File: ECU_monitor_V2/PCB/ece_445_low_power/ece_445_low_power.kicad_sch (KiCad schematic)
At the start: 59 parts, among them J1 Conn_01x02, J2 Conn_01x02, J3 Conn_02x02_Counter_Clockwise, J4 Conn_01x02, J5 LED, J6 ISP, Q1 2N7000, U1 LM393, U2 Si8640BD-B-IS2, U3 ATtiny85-20S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

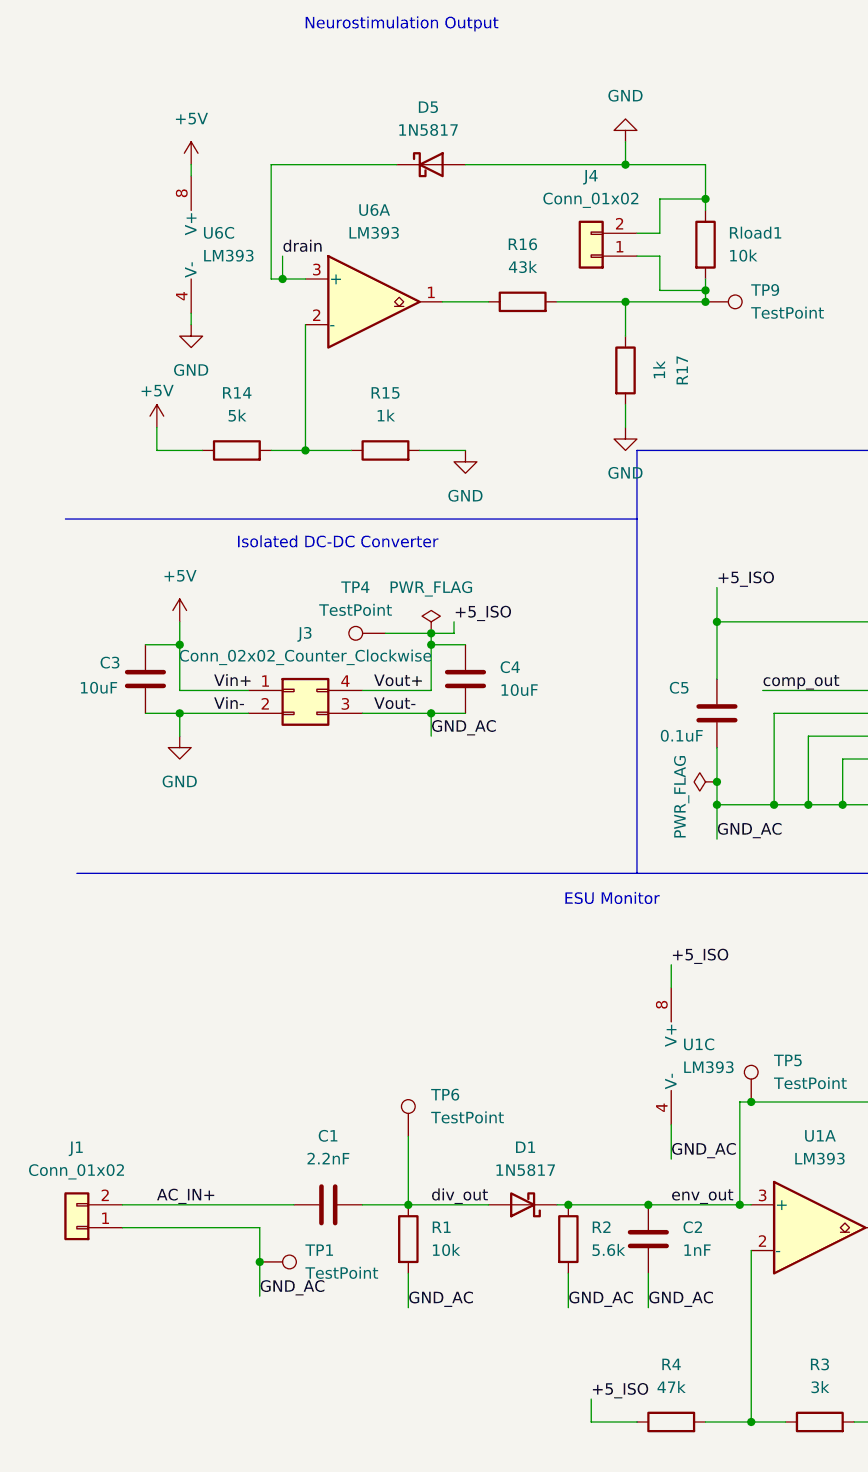
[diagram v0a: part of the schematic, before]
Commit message: Updated Low Power PCB, added missing 1k resistor to +5V in output
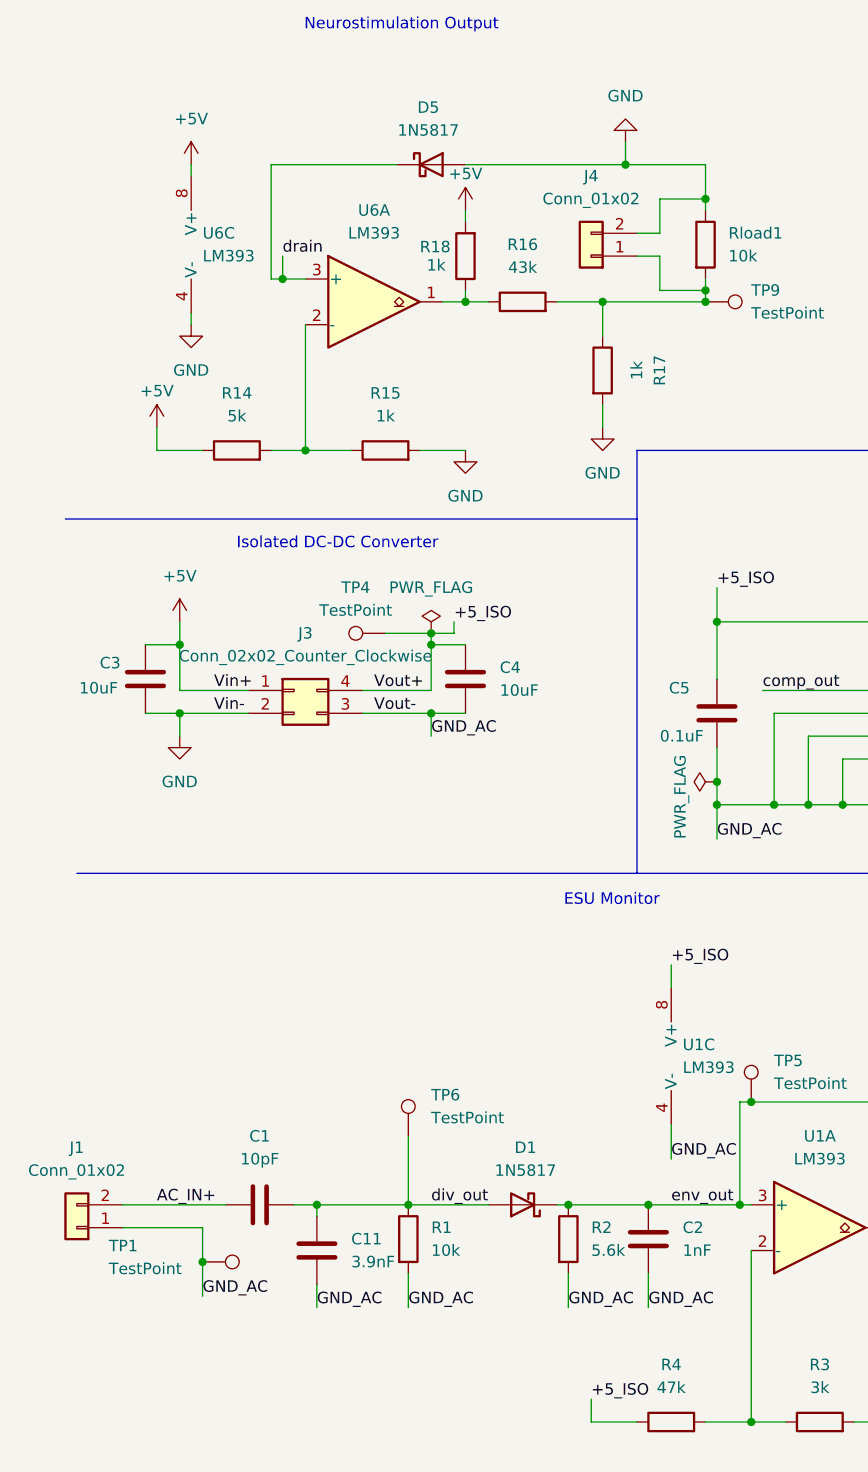
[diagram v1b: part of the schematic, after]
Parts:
- added C11: 3.9nF, Capacitor_THT:C_Disc_D4.7mm_W2.5mm_P5.00mm, symbol Device:C
- added R18: 1k, Resistor_THT:R_Axial_DIN0207_L6.3mm_D2.5mm_P10.16mm_Horizontal, symbol Device:R
- C1: value 2.2nF -> 10pF
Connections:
- net +5V: now also R18.2
- net GND_AC: now also C11.1
- net div_out: now also C11.2
- net at R16.1, U6.1: now also R18.1
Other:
- moved on the sheet: C1, R17, TP1
